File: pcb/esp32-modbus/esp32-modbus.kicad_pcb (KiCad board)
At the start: 2 copper layers, 85.8 x 77.9 mm, 54 parts, among them J1 Conn_01x01_Male, J10 Conn_01x01_Male, J12 Conn_01x01_Male, J13 Conn_01x01_Male, J2 Conn_01x05_Male, J22 Conn_01x01_Male, J23 Conn_01x01_Male, J24 Conn_01x01_Male, J25 Conn_01x01_Male, J26 Conn_01x01_Male, J27_VCC1 Conn_01x01_Male, J28_RO1 Conn_01x01_Male, J29_DI1 Conn_01x01_Male, J3 Conn_01x01_Male, J30_RE/DE1 Conn_01x01_Male, J31_GND1 Conn_01x01_Male, J4 Conn_01x01_Male, J5 Conn_01x01_Male, J6 Screw_Terminal_01x02, J7 Conn_01x09_Male, J8 Conn_01x09_Male, J9 Conn_01x01_Male, Q1 BC817, Q2 BC817, U1 ESP32-WROOM-32U

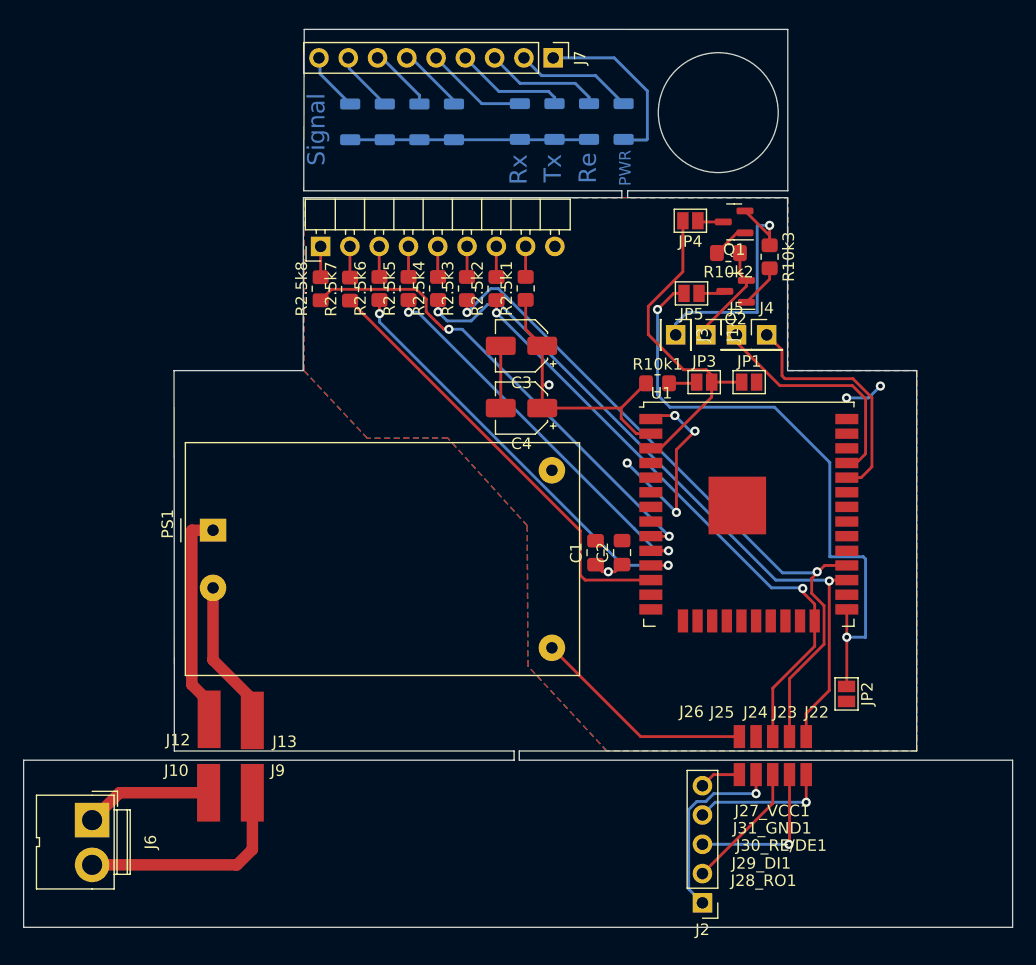
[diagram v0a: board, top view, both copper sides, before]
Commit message: pcb update, esp01 wifi
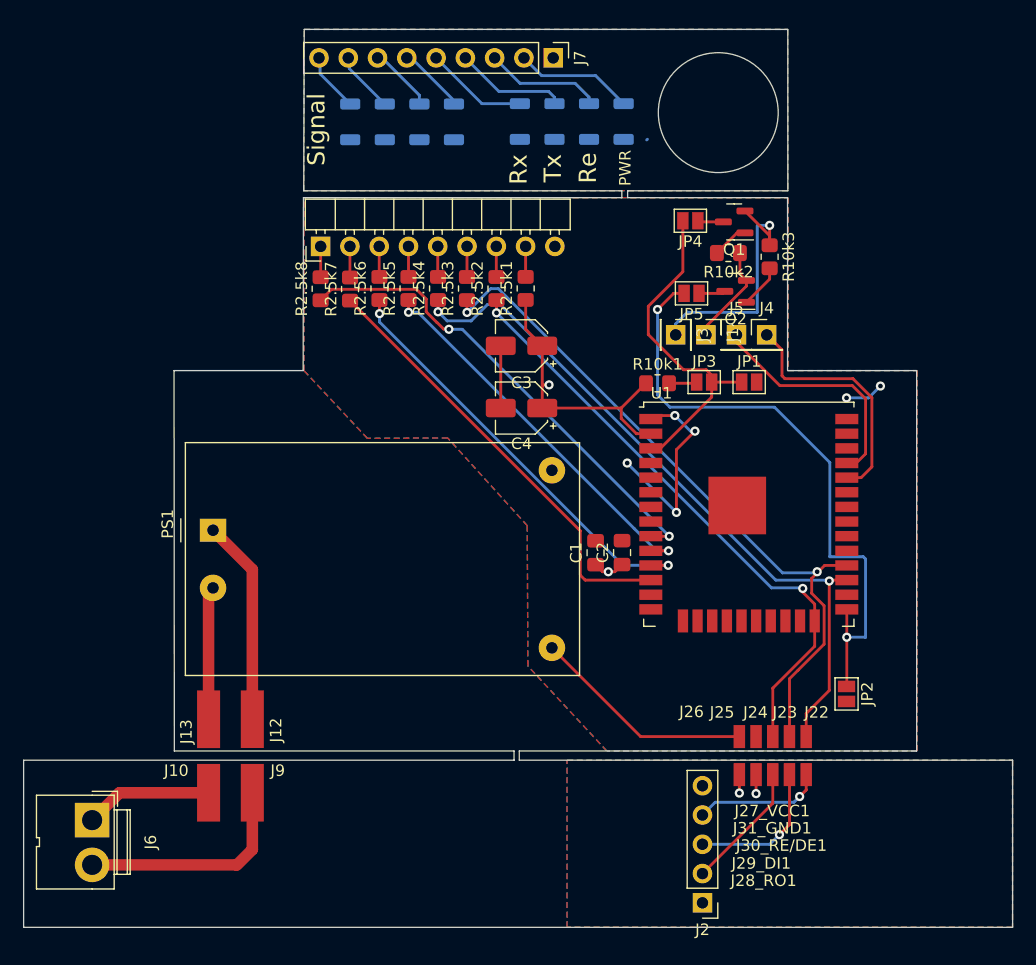
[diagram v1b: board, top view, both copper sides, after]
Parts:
- J8: footprint Connector_PinHeader_2.54mm:PinHeader_1x09_P2.54mm_Horizontal -> custom:PinHeader_1x09_P2.54mm_Horizontal
- moved J13 3.80 mm to (144.9, 129.6)
- moved J12 3.75 mm to (148.8, 129.6)
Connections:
- net Net-(D1-Pad1) renamed GND2
- net Net-(J2-Pad1) renamed GND1
- net Net-(J2-Pad5) renamed +3.3VA
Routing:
- net GND2: track 36.7 -> 0.16 mm
- net GND1: track 16.7 -> 1.65 mm
- net +3.3VA: track 3.60 -> 1.60 mm, vias 0 -> 1
- net Net-(J13-Pad1): track 12.9 -> 11.6 mm
- net Net-(J12-Pad1): track 18.9 -> 17.8 mm
- net Net-(J2-Pad3): track 13.6 -> 12.6 mm
- net Net-(J2-Pad4): track 11.9 -> 11.2 mm
- added copper zone on B.Cu, net +3.3VA
- added copper zone on F.Cu, net GND1
- added copper zone on B.Cu, net GND2
- added copper zone on F.Cu, net GND2

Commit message: update
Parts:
- J7: footprint Connector_PinHeader_2.54mm:PinHeader_1x09_P2.54mm_Vertical -> Connector_PinSocket_2.54mm:PinSocket_1x09_P2.54mm_Vertical; moved to B.Cu
- moved C2 15.8 mm to (179.2, 99.4), turned to 180 degrees
- moved C1 13.4 mm to (179.2, 101.7), turned to 180 degrees
- moved J27_VCC1 12.2 mm to (178.9, 136.0)
- moved J28_RO1 12.2 mm to (184.7, 136.0)
- moved J30_RE/DE1 12.2 mm to (181.8, 136.0)
- moved J29_DI1 12.2 mm to (183.2, 136.0)
- moved J31_GND1 12.2 mm to (180.3, 136.0)
- moved J22 12.1 mm to (184.7, 131.1)
- moved J24 12.1 mm to (181.8, 131.1)
- moved J26 12.1 mm to (178.9, 131.1)
- moved J23 12.1 mm to (183.2, 131.1)
- moved J25 12.1 mm to (180.3, 131.1)
- moved C3 11.0 mm to (181.1, 91.0)
- moved C4 9.97 mm to (179.5, 96.0)
- moved JP2 9.96 mm to (203.6, 118.0)
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- renumbered R2.5k3 to R2.5k
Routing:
- net GND: track 28.0 -> 66.8 mm, vias 6 -> 12
- net +3.3V: track 46.8 -> 60.6 mm, vias 2 -> 5
- net /TX: track 61.5 -> 71.0 mm, vias 2 -> 6
- net /GPIO0: track 54.0 -> 47.4 mm
- net Net-(J2-Pad4): track 11.2 -> 4.68 mm, vias 1 -> 0
- net /GPIO2: track 52.4 -> 58.4 mm, vias 2 -> 1
- net Net-(D2-Pad2): track 10.3 -> 16.2 mm, vias 0 -> 1
- net Net-(J2-Pad3): track 12.6 -> 7.12 mm, vias 1 -> 0
- net /GPIO27: track 38.4 -> 41.9 mm, vias 0 -> 3
- net /GPIO25: track 33.7 -> 30.6 mm
- net (no net): track 0.00 -> 2.88 mm
- net Net-(D1-Pad2): track 10.2 -> 12.8 mm, vias 0 -> 2
- net /GPIO33: track 41.8 -> 39.9 mm
- net Net-(D8-Pad2): track 5.39 -> 3.56 mm
- net Net-(J2-Pad2): track 11.1 -> 9.44 mm
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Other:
- board size 85.8 x 77.9 mm -> 77.5 x 77.9 mm
- board text added: "2.5k"
- board text added: "RTS DTR"
- board text added: "TX RX"

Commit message: update
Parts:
- moved J29_DI1 0.23 mm to (183.2, 136.3)
- moved J27_VCC1 0.23 mm to (178.9, 136.3)
- moved J28_RO1 0.23 mm to (184.7, 136.3)
- moved J30_RE/DE1 0.23 mm to (181.8, 136.3)
- moved J31_GND1 0.23 mm to (180.3, 136.3)
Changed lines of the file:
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@@
   )
   (footprint "custom:TestPoint_Pad_4.0x4.0mm2" (layer "F.Cu")
-    (at 183.24 136.03)
+    (at 183.23 136.26)
     (descr "SMD rectangular pad as test Point, square 4.0mm side length")
     (tags "test point SMD pad rectangle square")
@@
   )
   (footprint "custom:TestPoint_Pad_4.0x4.0mm2" (layer "F.Cu")
-    (at 178.89 136.03)
+    (at 178.88 136.26)
     (descr "SMD rectangular pad as test Point, square 4.0mm side length")
     (tags "test point SMD pad rectangle square")
@@
   )
   (footprint "custom:TestPoint_Pad_4.0x4.0mm2" (layer "F.Cu")
-    (at 184.69 136.03)
+    (at 184.68 136.26)
     (descr "SMD rectangular pad as test Point, square 4.0mm side length")
     (tags "test point SMD pad rectangle square")
@@
   )
   (footprint "custom:TestPoint_Pad_4.0x4.0mm2" (layer "F.Cu")
-    (at 181.79 136.03)
+    (at 181.78 136.26)
     (descr "SMD rectangular pad as test Point, square 4.0mm side length")
     (tags "test point SMD pad rectangle square")
@@
   )
   (footprint "custom:TestPoint_Pad_4.0x4.0mm2" (layer "F.Cu")
-    (at 180.34 136.03)
+    (at 180.33 136.26)
     (descr "SMD rectangular pad as test Point, square 4.0mm side length")
     (tags "test point SMD pad rectangle square")
@@
   (segment (start 172.26 74.11901) (end 173.435 72.94401) (width 0.25) (layer "B.Cu") (net 38))
   (segment (start 173.435 72.94401) (end 177.71401 72.94401) (width 0.25) (layer "B.Cu") (net 38))
-  (segment (start 181.74 135.98) (end 181.74 136.925) (width 0.25) (layer "F.Cu") (net 40))
-  (segment (start 181.74 136.925) (end 187.75 142.935) (width 0.25) (layer "F.Cu") (net 40))
-  (segment (start 186.355 140.395) (end 187.75 140.395) (width 0.25) (layer "F.Cu") (net 41))
-  (segment (start 183.19 137.23) (end 186.355 140.395) (width 0.25) (layer "F.Cu") (net 41))
-  (segment (start 183.19 135.98) (end 183.19 137.23) (width 0.25) (layer "F.Cu") (net 41))
-  (segment (start 184.64 135.98) (end 184.64 137.31) (width 0.25) (layer "F.Cu") (net 42))
+  (segment (start 182.0525 137.2375) (end 187.75 142.935) (width 0.25) (layer "F.Cu") (net 40))
+  (segment (start 181.73 136.915) (end 182.0525 137.2375) (width 0.25) (layer "F.Cu") (net 40))
+  (segment (start 181.73 136.21) (end 181.73 136.915) (width 0.25) (layer "F.Cu") (net 40))
+  (segment (start 182.0525 136.5325) (end 181.73 136.21) (width 0.25) (layer "F.Cu") (net 40))
+  (segment (start 183.18 137.22) (end 183.18 136.21) (width 0.25) (layer "F.Cu") (net 41))
+  (segment (start 187.75 140.395) (end 186.355 140.395) (width 0.25) (layer "F.Cu") (net 41))
+  (segment (start 186.355 140.395) (end 183.18 137.22) (width 0.25) (layer "F.Cu") (net 41))
+  (segment (start 184.64 137.31) (end 184.64 136.22) (width 0.25) (layer "F.Cu") (net 42))
   (segment (start 185.2 137.87) (end 185.215 137.855) (width 0.25) (layer "F.Cu") (net 42))
   (segment (start 185.215 137.855) (end 187.75 137.855) (width 0.25) (layer "F.Cu") (net 42))
+  (segment (start 184.64 136.22) (end 184.63 136.21) (width 0.25) (layer "F.Cu") (net 42))
   (segment (start 184.64 137.31) (end 185.2 137.87) (width 0.25) (layer "F.Cu") (net 42))
   (segment (start 178.84 135.98) (end 178.84 138.02) (width 0.25) (layer "F.Cu") (net 43))

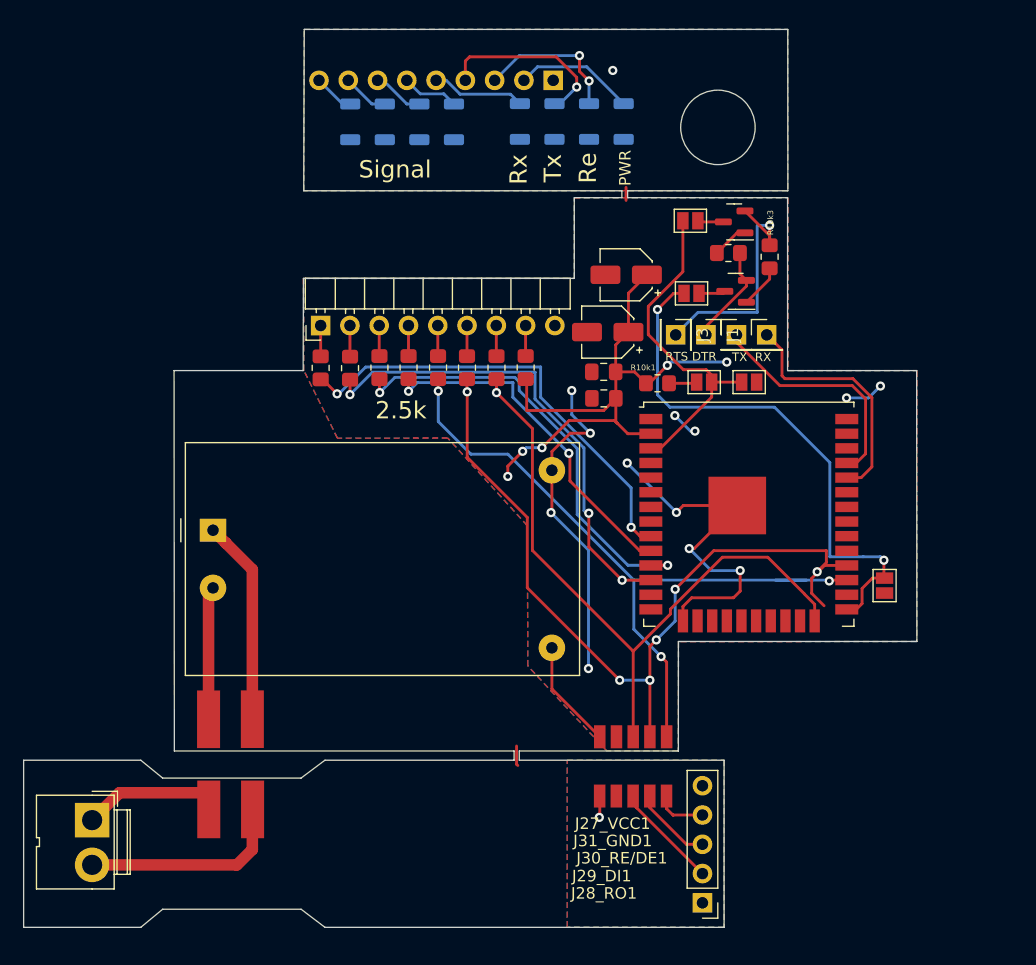
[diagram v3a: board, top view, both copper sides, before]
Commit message: signal strength diodes
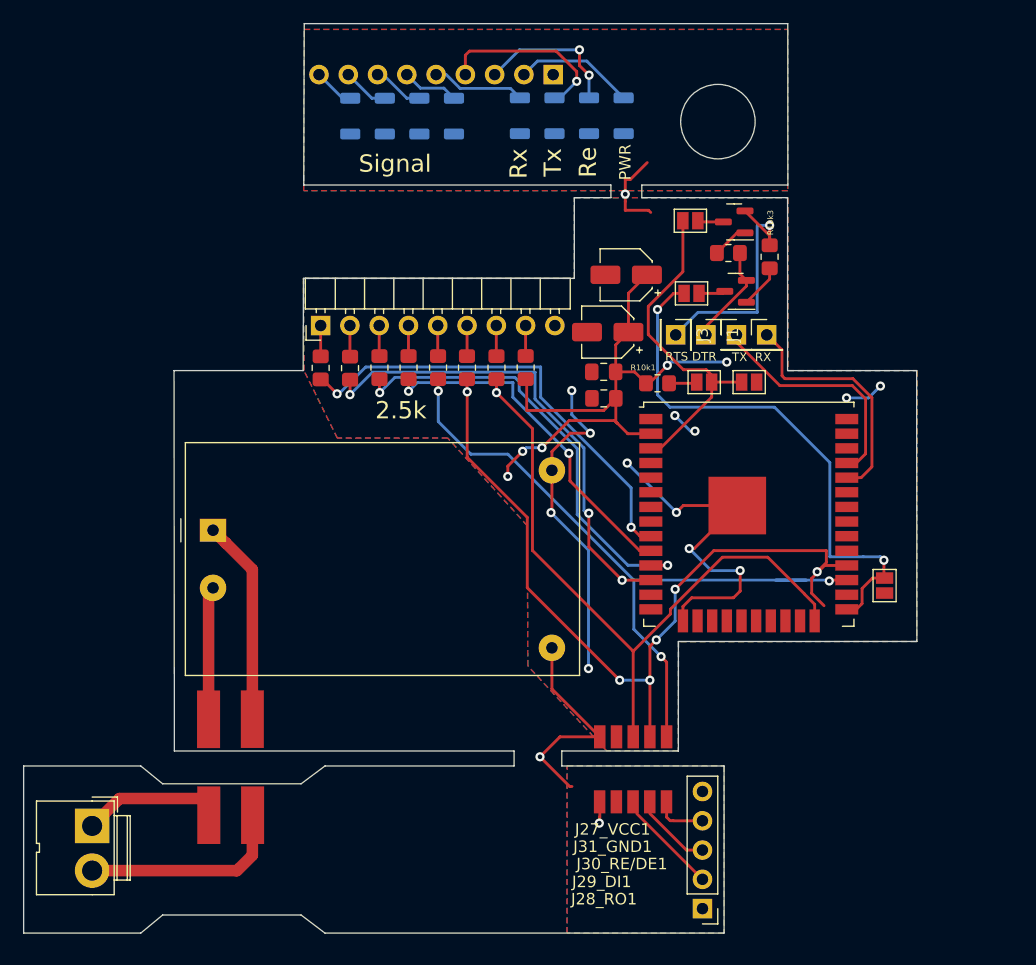
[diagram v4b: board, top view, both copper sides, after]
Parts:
- moved D1 0.50 mm to (177.9, 77.2)
- moved D2 0.50 mm to (174.9, 77.2)
- moved D3 0.50 mm to (171.9, 77.2)
- moved D4 0.50 mm to (180.9, 77.2)
- moved D5 0.50 mm to (166.2, 77.2)
- moved D6 0.50 mm to (163.2, 77.2)
- moved D7 0.50 mm to (160.2, 77.2)
- moved D8 0.50 mm to (157.2, 77.2)
- moved J10 0.50 mm to (145.0, 137.9)
- moved J2 0.50 mm to (187.8, 146.0)
- moved J27_VCC1 0.50 mm to (178.9, 136.8)
- moved J28_RO1 0.50 mm to (184.7, 136.8)
- moved J29_DI1 0.50 mm to (183.2, 136.8)
- moved J30_RE/DE1 0.50 mm to (181.8, 136.8)
- moved J31_GND1 0.50 mm to (180.3, 136.8)
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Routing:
- net +3.3V: track 60.6 -> 70.4 mm, vias 5 -> 6
- net GND2: track 0.07 -> 4.49 mm
- net GND: track 66.8 -> 69.9 mm
- net (no net): track 2.88 -> 0.00 mm
- net Net-(J2-Pad4): track 4.45 -> 5.66 mm
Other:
- board size 77.5 x 77.9 mm -> 77.5 x 78.9 mm
